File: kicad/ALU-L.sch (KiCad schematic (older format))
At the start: 45 parts, among them U36 4077, U37 74LS86, U38 74LS86, U39 74LS86, U40 74LS86, U41 74LS86, U42 74LS86, U43 74LS86, U44 74LS86, U45 4077, U46 4077, U47 4077, U48 4077, U49 4077, U50 4077, U51 4077, U52 74LS08, U53 74LS08, U54 74LS245, U55 74LS245, U56 74LS08, U57 74LS08, U58 74LS245, U59 74LS08, U60 74LS08, U61 74LS245, U62 74LS245, U63 74LS04, U64 74LS08, U65 74LS04, U66 74LS04, U67 74LS08, U68 74LS04, U69 74LS04, U70 74LS04, U71 74LS32, U72 74LS32, U73 74LS32, U74 74LS32, U75 74LS32, U76 74LS32, U77 74LS32, U78 74LS32, U79 74LS04, U80 74LS04

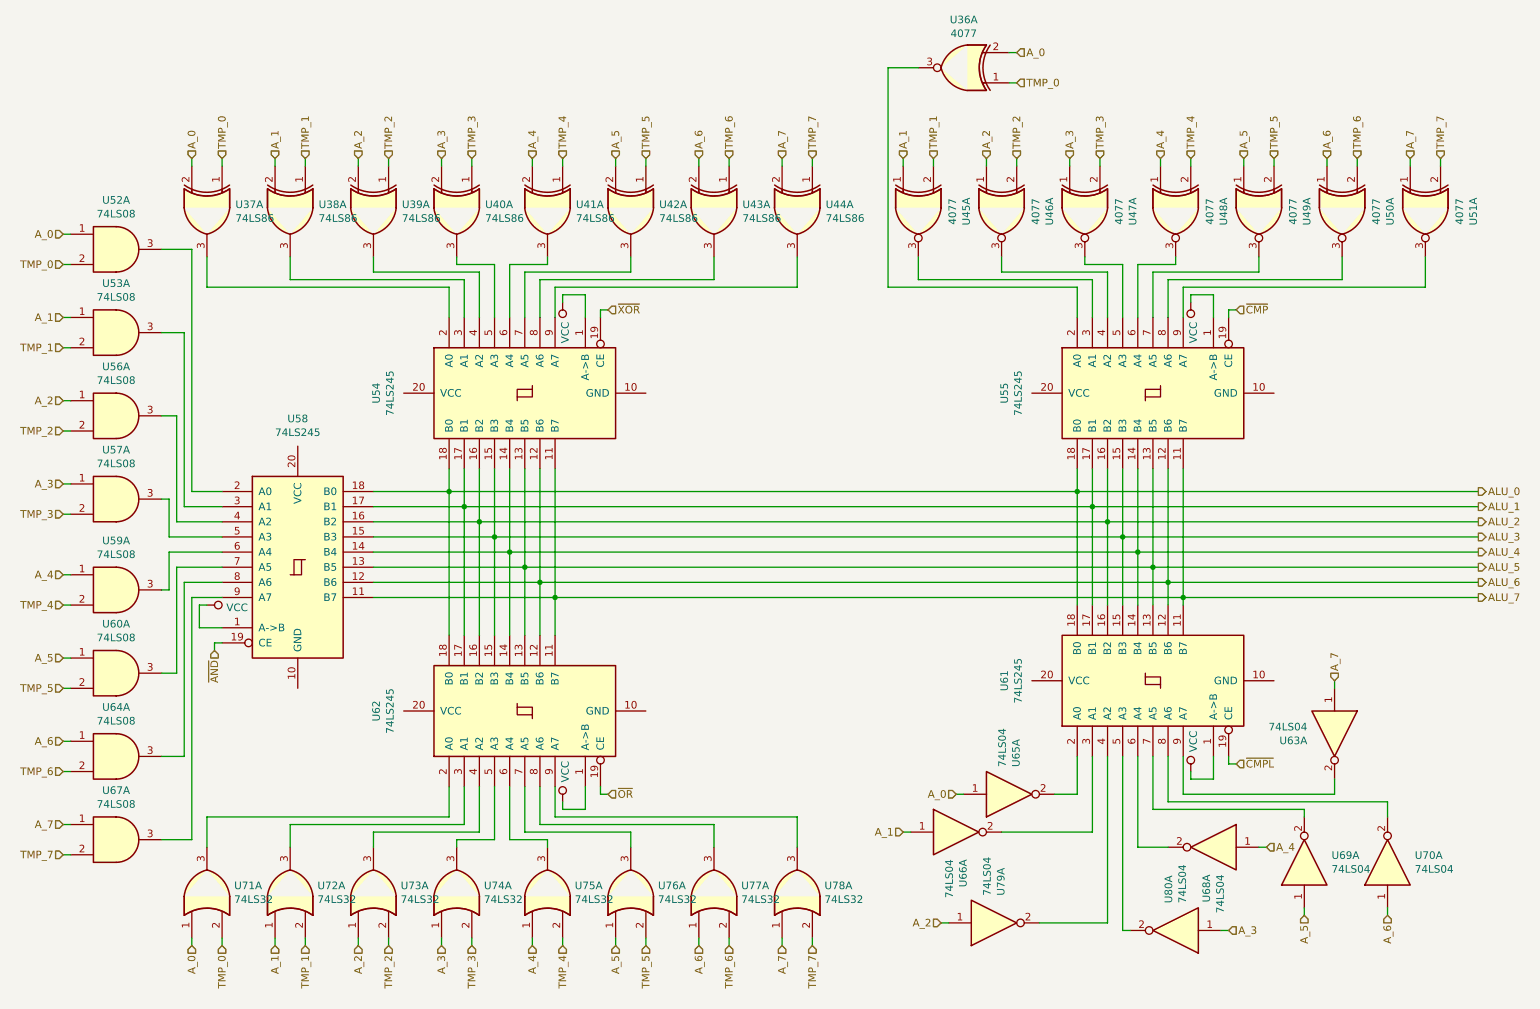
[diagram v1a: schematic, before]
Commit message: Reorganize part references
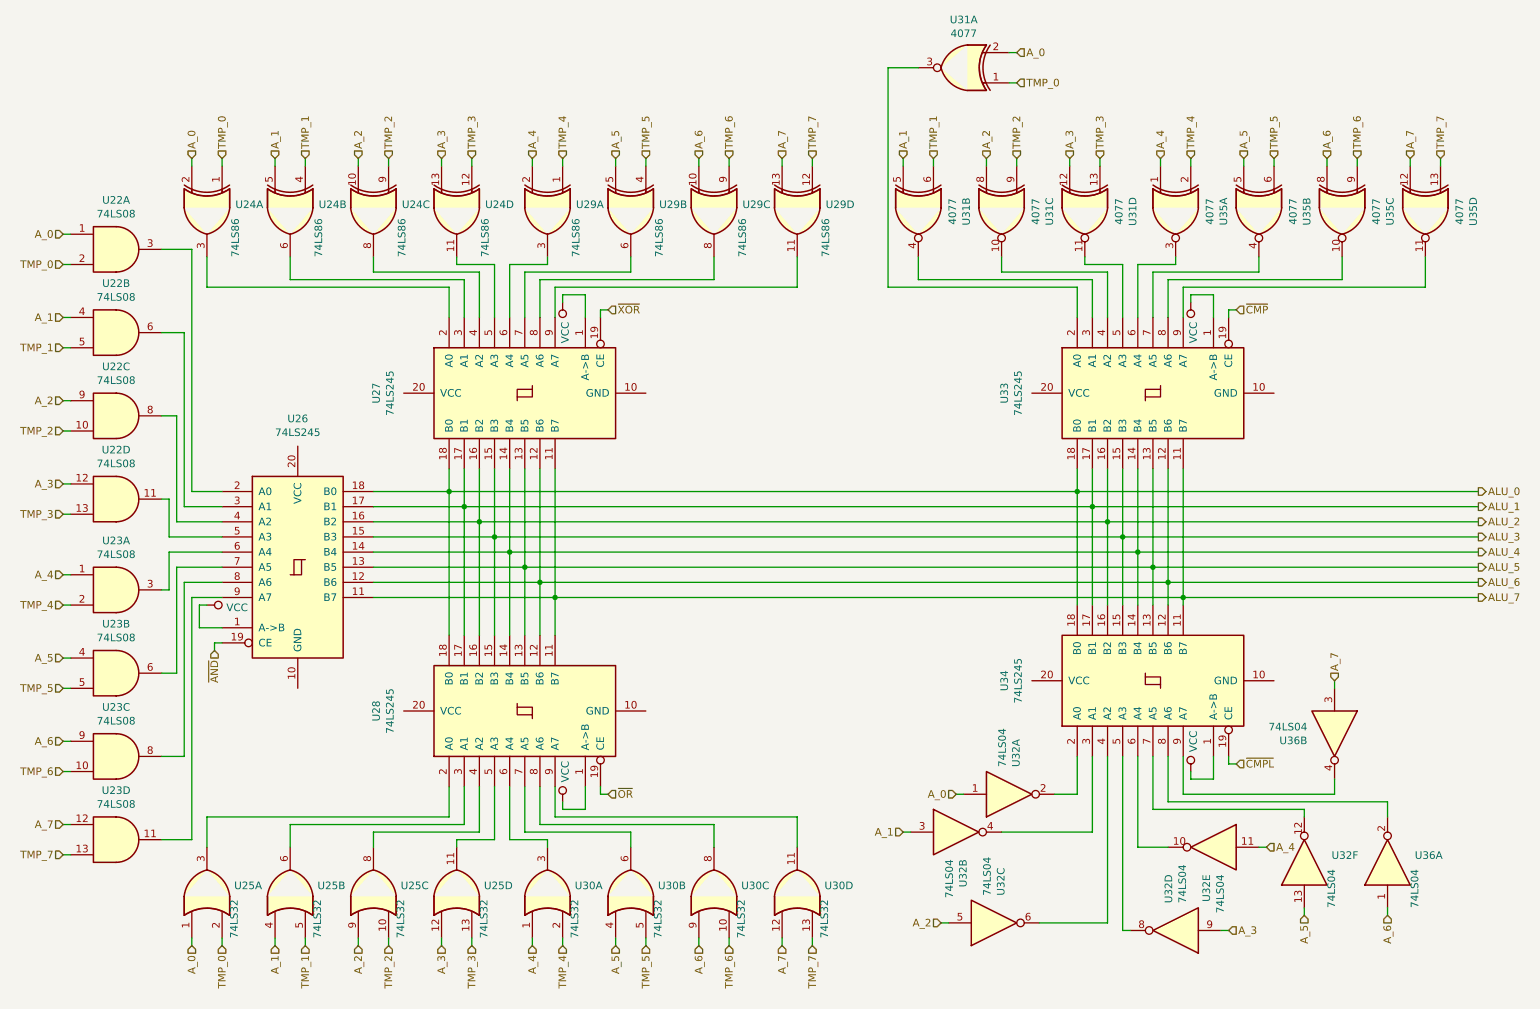
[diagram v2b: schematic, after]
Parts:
- renumbered U52 to U22, U53 to U22, U56 to U22, U57 to U22, U59 to U23, U60 to U23, U64 to U23, U67 to U23, U37 to U24, U38 to U24, U39 to U24, U40 to U24, U71 to U25, U72 to U25, U73 to U25, U74 to U25, U58 to U26, U54 to U27, U62 to U28, U41 to U29, U42 to U29, U43 to U29, U44 to U29, U75 to U30, U76 to U30, U77 to U30, U78 to U30, U36 to U31, U47 to U31, U46 to U31, U45 to U31, U65 to U32, U66 to U32, U79 to U32, U80 to U32, U68 to U32, U69 to U32, U55 to U33, U61 to U34, U50 to U35, U49 to U35, U48 to U35, U51 to U35, U70 to U36, U63 to U36
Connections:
- net A_1: now also U22.4, U24.5, U25.4, U31.5, U32.3; no longer U22.1, U24.2, U25.1, U31.1, U32.1
- net A_2: now also U22.9, U24.10, U25.9, U31.8, U32.5; no longer U22.1, U24.2, U25.1, U31.1, U32.1
- net A_3: now also U22.12, U24.13, U25.12, U31.12, U32.9; no longer U22.1, U24.2, U25.1, U31.1, U32.1
- net A_4: now also U32.11; no longer U32.1
- net A_5: now also U23.4, U29.5, U30.4, U32.13, U35.5; no longer U23.1, U29.2, U30.1, U32.1, U35.1
- net A_6: now also U23.9, U29.10, U30.9, U35.8; no longer U23.1, U29.2, U30.1, U35.1
- net A_7: now also U23.12, U29.13, U30.12, U35.12, U36.3; no longer U23.1, U29.2, U30.1, U35.1, U36.1
- net TMP_1: now also U22.5, U24.4, U25.5, U31.6; no longer U22.2, U24.1, U25.2, U31.2
- net TMP_2: now also U22.10, U24.9, U25.10, U31.9; no longer U22.2, U24.1, U25.2, U31.2
- net TMP_3: now also U22.13, U24.12, U25.13, U31.13; no longer U22.2, U24.1, U25.2, U31.2
- net TMP_5: now also U23.5, U29.4, U30.5, U35.6; no longer U23.2, U29.1, U30.2, U35.2
- net TMP_6: now also U23.10, U29.9, U30.10, U35.9; no longer U23.2, U29.1, U30.2, U35.2
- net TMP_7: now also U23.13, U29.12, U30.13, U35.13; no longer U23.2, U29.1, U30.2, U35.2
- net at U26.3 (A1): now also U22.6; no longer U22.3
- net at U26.4 (A2): now also U22.8; no longer U22.3
- net at U26.5 (A3): now also U22.11; no longer U22.3
- net at U26.7 (A5): now also U23.6; no longer U23.3
- net at U26.8 (A6): now also U23.8; no longer U23.3
- net at U26.9 (A7): now also U23.11; no longer U23.3
- net at U28.3 (A1): now also U25.6; no longer U25.3
- net at U28.4 (A2): now also U25.8; no longer U25.3
- net at U28.5 (A3): now also U25.11; no longer U25.3
- net at U28.7 (A5): now also U30.6; no longer U30.3
- net at U28.8 (A6): now also U30.8; no longer U30.3
- net at U28.9 (A7): now also U30.11; no longer U30.3
- net at U27.3 (A1): now also U24.6; no longer U24.3
- net at U27.4 (A2): now also U24.8; no longer U24.3
- net at U27.5 (A3): now also U24.11; no longer U24.3
- net at U27.7 (A5): now also U29.6; no longer U29.3
- net at U27.8 (A6): now also U29.8; no longer U29.3
- net at U27.9 (A7): now also U29.11; no longer U29.3
- net at U33.3 (A1): now also U31.4; no longer U31.3
- net at U33.4 (A2): now also U31.10; no longer U31.3
- net at U33.5 (A3): now also U31.11; no longer U31.3
- net at U33.7 (A5): now also U35.4; no longer U35.3
- net at U33.8 (A6): now also U35.10; no longer U35.3
- net at U33.9 (A7): now also U35.11; no longer U35.3
- net at U34.3 (A1): now also U32.4; no longer U32.2
- net at U34.4 (A2): now also U32.6; no longer U32.2
- net at U34.5 (A3): now also U32.8; no longer U32.2
- net at U34.6 (A4): now also U32.10; no longer U32.2
- net at U34.7 (A5): now also U32.12; no longer U32.2
- net at U34.9 (A7): now also U36.4; no longer U36.2

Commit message: Up to v1.0 and plot
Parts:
- removed U31, U35: 4077, symbol 4xxx:4077
- added U?: 74LS688, symbol 74xx:74LS688
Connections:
- net A_0: now also U?.2 (P0)
- net A_1: now also U?.4 (P1)
- net A_2: now also U?.6 (P2)
- net A_3: now also U?.8 (P3)
- net A_4: now also U?.11 (P4)
- net A_5: now also U?.13 (P5)
- net A_6: now also U?.15 (P6)
- net A_7: now also U?.17 (P7)
- net TMP_0: now also U?.3 (R0)
- net TMP_1: now also U?.5 (R1)
- net TMP_2: now also U?.7 (R2)
- net TMP_3: now also U?.9 (R3)
- net TMP_4: now also U?.12 (R4)
- net TMP_5: now also U?.14 (R5)
- net TMP_6: now also U?.16 (R6)
- net TMP_7: now also U?.18 (R7)
- net at U33.2 (A0): now also U33.3 (A1), U33.4 (A2), U33.5 (A3), U33.6 (A4), U33.7 (A5), U33.8 (A6), U33.9 (A7), U?.19 (P=R)
- new net GND: U?.1 (G)
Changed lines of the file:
@@
 encoding utf-8
 Sheet 8 26
-Title ""
-Date "2019-10-03"
-Rev "v0.1"
+Title "ALU Logic"
+Date "2019-11-13"
+Rev "v1.0"
 Comp "Christopher Milan"
 Comment1 "Computer Science 4"
@@
 Text HLabel 8600 5500 2    50   Input ~ 0
 ~CMPL~
-Text HLabel 7150 800  2    50   Input ~ 0
-A_0
-Wire Wire Line
-	7150 800  7100 800
 Wire Wire Line
 	8550 2500 8600 2500
@@
 	1    0    0    1
 $EndComp
-Wire Wire Line
-	7550 2350 6300 2350
-Wire Wire Line
-	7550 2550 7550 2350
-Wire Wire Line
-	7650 2300 7650 2550
-Wire Wire Line
-	6500 2300 7650 2300
-Wire Wire Line
-	6500 2150 6500 2300
-Wire Wire Line
-	7050 2250 7050 2150
-Wire Wire Line
-	7750 2250 7050 2250
-Wire Wire Line
-	7750 2550 7750 2250
-Wire Wire Line
-	8250 2350 8250 2550
-Wire Wire Line
-	9300 2300 9300 2150
-Wire Wire Line
-	8150 2300 9300 2300
-Wire Wire Line
-	8150 2550 8150 2300
-Wire Wire Line
-	8750 2250 8750 2150
-Wire Wire Line
-	8050 2250 8750 2250
-Wire Wire Line
-	8050 2550 8050 2250
-Wire Wire Line
-	7850 2200 7850 2550
-Wire Wire Line
-	7600 2200 7850 2200
-Wire Wire Line
-	7600 2150 7600 2200
-Wire Wire Line
-	7950 2200 7950 2550
-Wire Wire Line
-	8200 2200 7950 2200
-Wire Wire Line
-	8200 2150 8200 2200
 $Comp
 L 74xx:74LS245 U33
@@
 	0    -1   1    0
 $EndComp
-Wire Wire Line
-	7150 1000 7100 1000
-Wire Wire Line
-	6400 1500 6400 1550
-Wire Wire Line
-	6600 1500 6600 1550
-Wire Wire Line
-	6950 1500 6950 1550
-Wire Wire Line
-	7150 1500 7150 1550
-Wire Wire Line
-	7500 1500 7500 1550
-Wire Wire Line
-	7700 1500 7700 1550
-Wire Wire Line
-	8100 1500 8100 1550
-Wire Wire Line
-	8300 1500 8300 1550
-Wire Wire Line
-	8650 1500 8650 1550
-Wire Wire Line
-	8850 1500 8850 1550
-Wire Wire Line
-	9200 1500 9200 1550
-Wire Wire Line
-	9400 1500 9400 1550
-Text HLabel 6400 1500 1    50   Input ~ 0
+Text HLabel 7650 1350 1    50   Input ~ 0
 A_1
-Text HLabel 6950 1500 1    50   Input ~ 0
+Text HLabel 7750 1350 1    50   Input ~ 0
 A_2
-Text HLabel 7500 1500 1    50   Input ~ 0
+Text HLabel 7850 1350 1    50   Input ~ 0
 A_3
-Text HLabel 8100 1500 1    50   Input ~ 0
+Text HLabel 7950 1350 1    50   Input ~ 0
 A_4
-Text HLabel 8650 1500 1    50   Input ~ 0
+Text HLabel 8050 1350 1    50   Input ~ 0
 A_5
-Text HLabel 9200 1500 1    50   Input ~ 0
+Text HLabel 8150 1350 1    50   Input ~ 0
 A_6
-Text HLabel 9400 1500 1    50   Input ~ 0
-TMP_6
-Text HLabel 8850 1500 1    50   Input ~ 0
-TMP_5
-Text HLabel 8300 1500 1    50   Input ~ 0
-TMP_4
-Text HLabel 7700 1500 1    50   Input ~ 0
-TMP_3
-Text HLabel 7150 1500 1    50   Input ~ 0
-TMP_2
-Text HLabel 6600 1500 1    50   Input ~ 0
-TMP_1
-Text HLabel 7150 1000 2    50   Input ~ 0
-TMP_0
 Wire Wire Line
 	3400 2350 1800 2350
@@
 Text HLabel 1700 1500 1    50   Input ~ 0
 A_0
-Wire Wire Line
-	9850 2350 8250 2350
-Text HLabel 9950 1500 1    50   Input ~ 0
-TMP_7
-Text HLabel 9750 1500 1    50   Input ~ 0
+Text HLabel 8250 1350 1    50   Input ~ 0
 A_7
-Wire Wire Line
-	9950 1500 9950 1550
-Wire Wire Line
-	9750 1500 9750 1550
-Wire Wire Line
-	9850 2150 9850 2350
-Wire Wire Line
-	6500 900  6300 900
-Wire Wire Line
-	6300 900  6300 2350
-$Comp
-L 4xxx:4077 U31
-U 1 1 5F1140E9
-P 6800 900
-F 0 "U31" H 6800 583 50  0000 C CNN
-F 1 "4077" H 6800 674 50  0000 C CNN
-F 2 "" H 6800 900 50  0001 C CNN
-F 3 "http://www.intersil.com/content/dam/Intersil/documents/cd40/cd4076bms.pdf" H 6800 900 50  0001 C CNN
-	1    6800 900
-	-1   0    0    1
-$EndComp
-$Comp
-L 4xxx:4077 U35
-U 3 1 5F12018D
-P 9300 1850
-F 0 "U35" H 9300 1533 50  0000 C CNN
-F 1 "4077" H 9300 1624 50  0000 C CNN
-F 2 "" H 9300 1850 50  0001 C CNN
-F 3 "http://www.intersil.com/content/dam/Intersil/documents/cd40/cd4076bms.pdf" H 9300 1850 50  0001 C CNN
-	3    9300 1850
-	0    -1   1    0
-$EndComp
-$Comp
-L 4xxx:4077 U35
-U 2 1 5F12D254
-P 8750 1850
-F 0 "U35" H 8750 1533 50  0000 C CNN
-F 1 "4077" H 8750 1624 50  0000 C CNN
-F 2 "" H 8750 1850 50  0001 C CNN
-F 3 "http://www.intersil.com/content/dam/Intersil/documents/cd40/cd4076bms.pdf" H 8750 1850 50  0001 C CNN
-	2    8750 1850
-	0    -1   1    0
-$EndComp
-$Comp
-L 4xxx:4077 U35
-U 1 1 5F141E58
-P 8200 1850
-F 0 "U35" H 8200 1533 50  0000 C CNN
-F 1 "4077" H 8200 1624 50  0000 C CNN
-F 2 "" H 8200 1850 50  0001 C CNN
-F 3 "http://www.intersil.com/content/dam/Intersil/documents/cd40/cd4076bms.pdf" H 8200 1850 50  0001 C CNN
-	1    8200 1850
-	0    -1   1    0
-$EndComp
-$Comp
-L 4xxx:4077 U31
-U 4 1 5F141E5E
-P 7600 1850
-F 0 "U31" H 7600 1533 50  0000 C CNN
-F 1 "4077" H 7600 1624 50  0000 C CNN
-F 2 "" H 7600 1850 50  0001 C CNN
-F 3 "http://www.intersil.com/content/dam/Intersil/documents/cd40/cd4076bms.pdf" H 7600 1850 50  0001 C CNN
-	4    7600 1850
-	0    -1   1    0
-$EndComp
-$Comp
-L 4xxx:4077 U31
-U 3 1 5F1544EA
-P 7050 1850
-F 0 "U31" H 7050 1533 50  0000 C CNN
-F 1 "4077" H 7050 1624 50  0000 C CNN
-F 2 "" H 7050 1850 50  0001 C CNN
-F 3 "http://www.intersil.com/content/dam/Intersil/documents/cd40/cd4076bms.pdf" H 7050 1850 50  0001 C CNN
-	3    7050 1850
-	0    -1   1    0
-$EndComp
-$Comp
-L 4xxx:4077 U31
-U 2 1 5F1544F0
-P 6500 1850
-F 0 "U31" H 6500 1533 50  0000 C CNN
-F 1 "4077" H 6500 1624 50  0000 C CNN
-F 2 "" H 6500 1850 50  0001 C CNN
-F 3 "http://www.intersil.com/content/dam/Intersil/documents/cd40/cd4076bms.pdf" H 6500 1850 50  0001 C CNN
-	2    6500 1850
-	0    -1   1    0
-$EndComp
-$Comp
-L 4xxx:4077 U35
-U 4 1 5F188260
-P 9850 1850
-F 0 "U35" H 9850 1533 50  0000 C CNN
-F 1 "4077" H 9850 1624 50  0000 C CNN
-F 2 "" H 9850 1850 50  0001 C CNN
-F 3 "http://www.intersil.com/content/dam/Intersil/documents/cd40/cd4076bms.pdf" H 9850 1850 50  0001 C CNN
-	4    9850 1850
-	0    -1   1    0
-$EndComp
 Wire Wire Line
 	7550 3550 7550 3700
@@
 	0    1    1    0
 $EndComp
+$Comp
+L 74xx:74LS688 U?
+U 1 1 5DAF0CC2
+P 8450 1950
+F 0 "U?" V 8404 706 50  0000 R CNN
+F 1 "74LS688" V 8495 706 50  0000 R CNN
+F 2 "" H 8450 1950 50  0001 C CNN
+F 3 "http://www.ti.com/lit/gpn/sn74LS688" H 8450 1950 50  0001 C CNN
+	1    8450 1950
+	0    -1   1    0
+$EndComp
+Text HLabel 7550 1350 1    50   Input ~ 0
+A_0
+Text HLabel 8450 1350 1    50   Input ~ 0
+TMP_0
+Text HLabel 9150 1350 1    50   Input ~ 0
+TMP_7
+Text HLabel 8550 1350 1    50   Input ~ 0
+TMP_1
+Text HLabel 8650 1350 1    50   Input ~ 0
+TMP_2
+Text HLabel 8750 1350 1    50   Input ~ 0
+TMP_3
+Text HLabel 8850 1350 1    50   Input ~ 0
+TMP_4
+Text HLabel 8950 1350 1    50   Input ~ 0
+TMP_5
+Text HLabel 9050 1350 1    50   Input ~ 0
+TMP_6
+Wire Wire Line
+	7650 2500 7650 2550
+Wire Wire Line
+	7550 2450 7550 2500
+Wire Wire Line
+	7650 2500 7550 2500
+Connection ~ 7550 2500
+Wire Wire Line
+	7550 2500 7550 2550
+Wire Wire Line
+	7650 2500 7750 2500
+Wire Wire Line
+	7750 2500 7750 2550
+Connection ~ 7650 2500
+Wire Wire Line
+	7750 2500 7850 2500
+Wire Wire Line
+	7850 2500 7850 2550
+Connection ~ 7750 2500
+Wire Wire Line
+	7850 2500 7950 2500
+Wire Wire Line
+	7950 2500 7950 2550
+Connection ~ 7850 2500
+Wire Wire Line
+	7950 2500 8050 2500
+Wire Wire Line
+	8050 2500 8050 2550
+Connection ~ 7950 2500
+Wire Wire Line
+	8050 2500 8150 2500
+Wire Wire Line
+	8150 2500 8150 2550
+Connection ~ 8050 2500
+Wire Wire Line
+	8150 2500 8250 2500
+Wire Wire Line
+	8250 2500 8250 2550
+Connection ~ 8150 2500
+Wire Wire Line
+	7550 1350 7550 1450
+Wire Wire Line
+	7650 1350 7650 1450
+Wire Wire Line
+	7750 1350 7750 1450
+Wire Wire Line
+	7850 1350 7850 1450
+Wire Wire Line
+	7950 1350 7950 1450
+Wire Wire Line
+	8050 1350 8050 1450
+Wire Wire Line
+	8150 1350 8150 1450
+Wire Wire Line
+	8250 1350 8250 1450
+Wire Wire Line
+	8450 1350 8450 1450
+Wire Wire Line
+	8550 1350 8550 1450
+Wire Wire Line
+	8650 1350 8650 1450
+Wire Wire Line
+	8750 1350 8750 1450
+Wire Wire Line
+	8850 1350 8850 1450
+Wire Wire Line
+	8950 1350 8950 1450
+Wire Wire Line
+	9050 1350 9050 1450
+Wire Wire Line
+	9150 1350 9150 1450
+$Comp
+L power:GND #PWR?
+U 1 1 5DFDB9D4
+P 9350 1350
+F 0 "#PWR?" H 9350 1100 50  0001 C CNN
+F 1 "GND" H 9355 1177 50  0000 C CNN
+F 2 "" H 9350 1350 50  0001 C CNN
+F 3 "" H 9350 1350 50  0001 C CNN
+	1    9350 1350
+	-1   0    0    1
+$EndComp
+Wire Wire Line
+	9350 1350 9350 1450
 $EndSCHEMATC
